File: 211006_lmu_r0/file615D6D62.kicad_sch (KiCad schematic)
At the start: 23 parts, among them U1 R-78C5.0-1.0

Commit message: Updated lmu project with relative library paths and fixed broken symbols
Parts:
- C1: symbol Device:CP1 -> Device:C_Polarized_US
- L1: symbol Device:L_Core_Ferrite_Coupled -> Device:L_Ferrite_Coupled
- PS1: MANUFACTURER (none) -> RECOM; STANDARD (none) -> Manufacturer Recommendations
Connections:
- net 0V_ISO is gone; now on net GND: C6.2, PS1.4 (-VOUT), TP7.1
- net 3.3V_ISO is gone; now on net +3V3: C6.1, PS1.5 (+VOUT), TP6.1
- net GND: now also D4.1 (K)
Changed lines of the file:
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@@
       (effects (font (size 1.27 1.27)) hide)
     )
+    (pin "1")
   )
   (symbol (lib_id "gnd_iso:GND_ISO") (at 237.49 72.39 0) (unit 1)
@@
       (effects (font (size 1.27 1.27)) hide)
     )
+    (pin "1")
   )
   (symbol (lib_id "gnd_iso:GND_ISO") (at 229.87 104.14 0) (unit 1)
@@
       (effects (font (size 1.27 1.27)) hide)
     )
+    (pin "1")
   )
   (symbol (lib_id "Regulator_Switching:R-78C5.0-1.0") (at 166.37 59.69 0) (unit 1)
@@
       (effects (font (size 1.27 1.27)) (justify left bottom) hide)
     )
-    (property "MANUFACTURER" "" (id 4) (at 213.36 64.77 0)
+    (property "MANUFACTURER" "RECOM" (id 4) (at 213.36 64.77 0)
       (effects (font (size 1.27 1.27)) (justify left bottom) hide)
     )
@@
       (effects (font (size 1.27 1.27)) (justify left bottom) hide)
     )
-    (property "STANDARD" "" (id 6) (at 213.36 64.77 0)
+    (property "STANDARD" "Manufacturer Recommendations" (id 6) (at 213.36 64.77 0)
       (effects (font (size 1.27 1.27)) (justify left bottom) hide)
     )
@@
     (pin "8")
   )
-  (symbol (lib_id "Device:L_Core_Ferrite_Coupled") (at 123.19 63.5 0) (unit 1)
+  (symbol (lib_id "Device:L_Ferrite_Coupled") (at 123.19 63.5 0) (unit 1)
     (in_bom yes) (on_board yes)
     (property "Reference" "L1" (id 0) (at 123.19 56.3626 0))
@@
     (pin "2")
   )
-  (symbol (lib_id "Device:CP1") (at 93.98 63.5 0) (unit 1)
+  (symbol (lib_id "Device:C_Polarized_US") (at 93.98 63.5 0) (unit 1)
     (in_bom yes) (on_board yes)
     (property "Reference" "C1" (id 0) (at 96.901 62.3316 0)

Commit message: Updated some components to make sourcing easier
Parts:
- C2, C3, C4, C5, C6, R1, R2: Manufacturer (none) -> -; Part Number (none) -> -
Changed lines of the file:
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@@
+      (effects (font (size 1.27 1.27)) hide)
+    )
+    (property "Part Number" "-" (id 4) (at 237.49 64.77 0)
+      (effects (font (size 1.27 1.27)) hide)
+    )
+    (property "Manufacturer" "-" (id 5) (at 237.49 64.77 0)
       (effects (font (size 1.27 1.27)) hide)
     )
@@
       (effects (font (size 1.27 1.27)) hide)
     )
+    (property "Part Number" "-" (id 4) (at 179.07 64.77 0)
+      (effects (font (size 1.27 1.27)) hide)
+    )
+    (property "Manufacturer" "-" (id 5) (at 179.07 64.77 0)
+      (effects (font (size 1.27 1.27)) hide)
+    )
     (pin "1")
     (pin "2")
@@
       (effects (font (size 1.27 1.27)) hide)
     )
+    (property "Part Number" "-" (id 4) (at 191.77 64.77 0)
+      (effects (font (size 1.27 1.27)) hide)
+    )
+    (property "Manufacturer" "-" (id 5) (at 191.77 64.77 0)
+      (effects (font (size 1.27 1.27)) hide)
+    )
     (pin "1")
     (pin "2")
@@
       (effects (font (size 1.27 1.27)) hide)
     )
+    (property "Part Number" "-" (id 4) (at 107.95 63.5 0)
+      (effects (font (size 1.27 1.27)) hide)
+    )
+    (property "Manufacturer" "-" (id 5) (at 107.95 63.5 0)
+      (effects (font (size 1.27 1.27)) hide)
+    )
     (pin "1")
     (pin "2")
@@
     )
     (property "Datasheet" "~" (id 3) (at 135.89 63.5 0)
+      (effects (font (size 1.27 1.27)) hide)
+    )
+    (property "Part Number" "-" (id 4) (at 135.89 63.5 0)
+      (effects (font (size 1.27 1.27)) hide)
+    )
+    (property "Manufacturer" "-" (id 5) (at 135.89 63.5 0)
       (effects (font (size 1.27 1.27)) hide)
     )
@@
       (effects (font (size 1.27 1.27)) hide)
     )
+    (property "Part Number" "-" (id 4) (at 229.87 92.71 0)
+      (effects (font (size 1.27 1.27)) hide)
+    )
+    (property "Manufacturer" "-" (id 5) (at 229.87 92.71 0)
+      (effects (font (size 1.27 1.27)) hide)
+    )
     (pin "1")
     (pin "2")
@@
       (effects (font (size 1.27 1.27)) hide)
     )
+    (property "Part Number" "-" (id 4) (at 204.47 92.71 0)
+      (effects (font (size 1.27 1.27)) hide)
+    )
+    (property "Manufacturer" "-" (id 5) (at 204.47 92.71 0)
+      (effects (font (size 1.27 1.27)) hide)
+    )

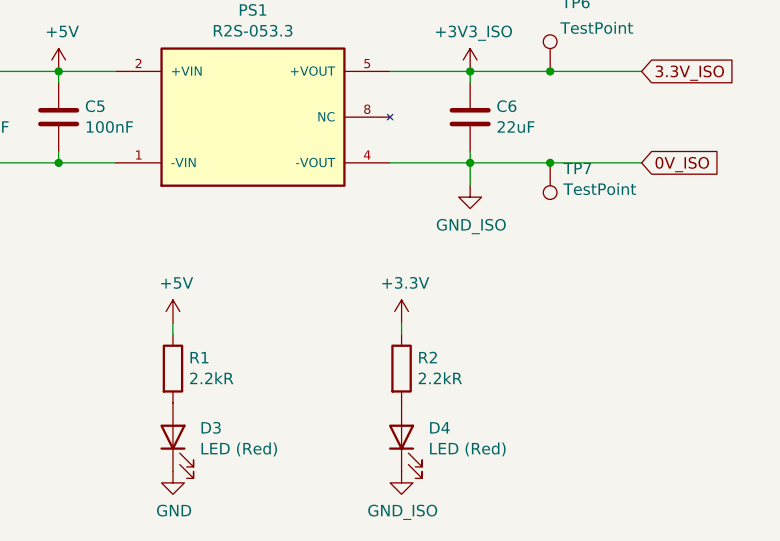
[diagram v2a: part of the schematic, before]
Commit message: fixed footprints for headers, started planning out zones
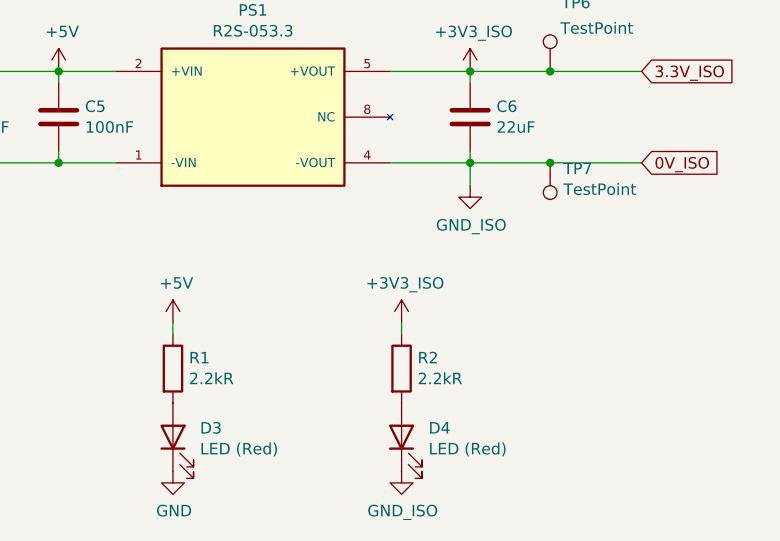
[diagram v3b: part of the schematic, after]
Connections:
- net GND: no longer C6.2, D4.1 (K), PS1.4 (-VOUT), TP7.1
- net +3V3 renamed +3V3_ISO
- new net GND_ISO: C6.2, D4.1 (K), PS1.4 (-VOUT), TP7.1
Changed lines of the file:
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@@
     (pin "1")
   )
-  (symbol (lib_id "gnd_iso:GND_ISO") (at 237.49 72.39 0) (unit 1)
+  (symbol (lib_name "GND_ISO_1") (lib_id "gnd_iso:GND_ISO") (at 237.49 72.39 0) (unit 1)
     (in_bom yes) (on_board yes)
     (property "Reference" "#PWR09" (id 0) (at 237.49 78.74 0)
@@
     (pin "2")
   )
-  (symbol (lib_id "power:+3.3V") (at 229.87 87.63 0) (unit 1)
-    (in_bom yes) (on_board yes)
-    (property "Reference" "#PWR06" (id 0) (at 229.87 91.44 0)
-      (effects (font (size 1.27 1.27)) hide)
-    )
-    (property "Value" "+3.3V" (id 1) (at 230.251 83.2358 0))
-    (property "Footprint" "" (id 2) (at 229.87 87.63 0)
-      (effects (font (size 1.27 1.27)) hide)
-    )
-    (property "Datasheet" "" (id 3) (at 229.87 87.63 0)
-      (effects (font (size 1.27 1.27)) hide)
-    )
-    (pin "1")
-  )
   (symbol (lib_id "Device:R") (at 204.47 92.71 0) (unit 1)
     (in_bom yes) (on_board yes)
@@
     (pin "2")
   )
+  (symbol (lib_name "+3V3_ISO_1") (lib_id "+3v3_iso:+3V3_ISO") (at 229.87 87.63 0) (unit 1)
+    (in_bom yes) (on_board yes)
+    (property "Reference" "#PWR0106" (id 0) (at 229.87 91.44 0)
+      (effects (font (size 1.27 1.27)) hide)
+    )
+    (property "Value" "+3V3_ISO" (id 1) (at 230.251 83.2358 0))
+    (property "Footprint" "" (id 2) (at 229.87 87.63 0)
+      (effects (font (size 1.27 1.27)) hide)
+    )
+    (property "Datasheet" "" (id 3) (at 229.87 87.63 0)
+      (effects (font (size 1.27 1.27)) hide)
+    )
+    (pin "1")
+  )
 )

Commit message: Lots of routing and placing, according to planned layout
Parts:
- F1: footprint Fuse:Fuse_2920_7451Metric_Castellated -> Fuse:Fuse_2920_7451Metric_Pad2.10x5.45mm_HandSolder
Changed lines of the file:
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@@
     (property "Reference" "F1" (id 0) (at 57.15 53.975 90))
     (property "Value" "Polyfuse 1A" (id 1) (at 57.15 56.2864 90))
-    (property "Footprint" "Fuse:Fuse_2920_7451Metric_Castellated" (id 2) (at 62.23 58.42 0)
+    (property "Footprint" "Fuse:Fuse_2920_7451Metric_Pad2.10x5.45mm_HandSolder" (id 2) (at 62.23 58.42 0)
       (effects (font (size 1.27 1.27)) (justify left) hide)
     )

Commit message: updated pcb still need to find j11
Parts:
- C5: footprint Capacitor_SMD:C_0603_1608Metric_Pad1.08x0.95mm_HandSolder -> Capacitor_SMD:C_0805_2012Metric_Pad1.18x1.45mm_HandSolder
- L1: symbol Device:L_Ferrite_Coupled -> Device:L_Coupled_1243
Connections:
- net GND: now also L1.3; no longer L1.4
- net VGND: now also L1.4; no longer L1.3
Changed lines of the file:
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@@
     (stroke (width 0) (type default) (color 0 0 0 0))
+  )
+  (polyline (pts (xy 213.36 12.7) (xy 213.36 198.12))
+    (stroke (width 0) (type default) (color 255 0 0 1))
   )
   (wire (pts (xy 135.89 69.85) (xy 143.51 69.85))
@@
     (pin "8")
   )
-  (symbol (lib_id "Device:L_Ferrite_Coupled") (at 123.19 63.5 0) (unit 1)
+  (symbol (lib_id "Device:L_Coupled_1243") (at 123.19 63.5 0) (unit 1)
     (in_bom yes) (on_board yes)
     (property "Reference" "L1" (id 0) (at 123.19 56.3626 0))
@@
       (effects (font (size 1.27 1.27)) (justify left))
     )
-    (property "Footprint" "Capacitor_SMD:C_0603_1608Metric_Pad1.08x0.95mm_HandSolder" (id 2) (at 192.7352 68.58 0)
-      (effects (font (size 1.27 1.27)) hide)
+    (property "Footprint" "Capacitor_SMD:C_0805_2012Metric_Pad1.18x1.45mm_HandSolder" (id 2) (at 192.7352 68.58 0)
+      (effects (font (size 1.27 1.27) bold) hide)
     )
     (property "Datasheet" "~" (id 3) (at 191.77 64.77 0)
